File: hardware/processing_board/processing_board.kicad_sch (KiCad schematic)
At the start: 8 parts, among them J1 USB_C_Receptacle_USB2.0_14P, J2 USB_C_Receptacle_USB2.0_14P

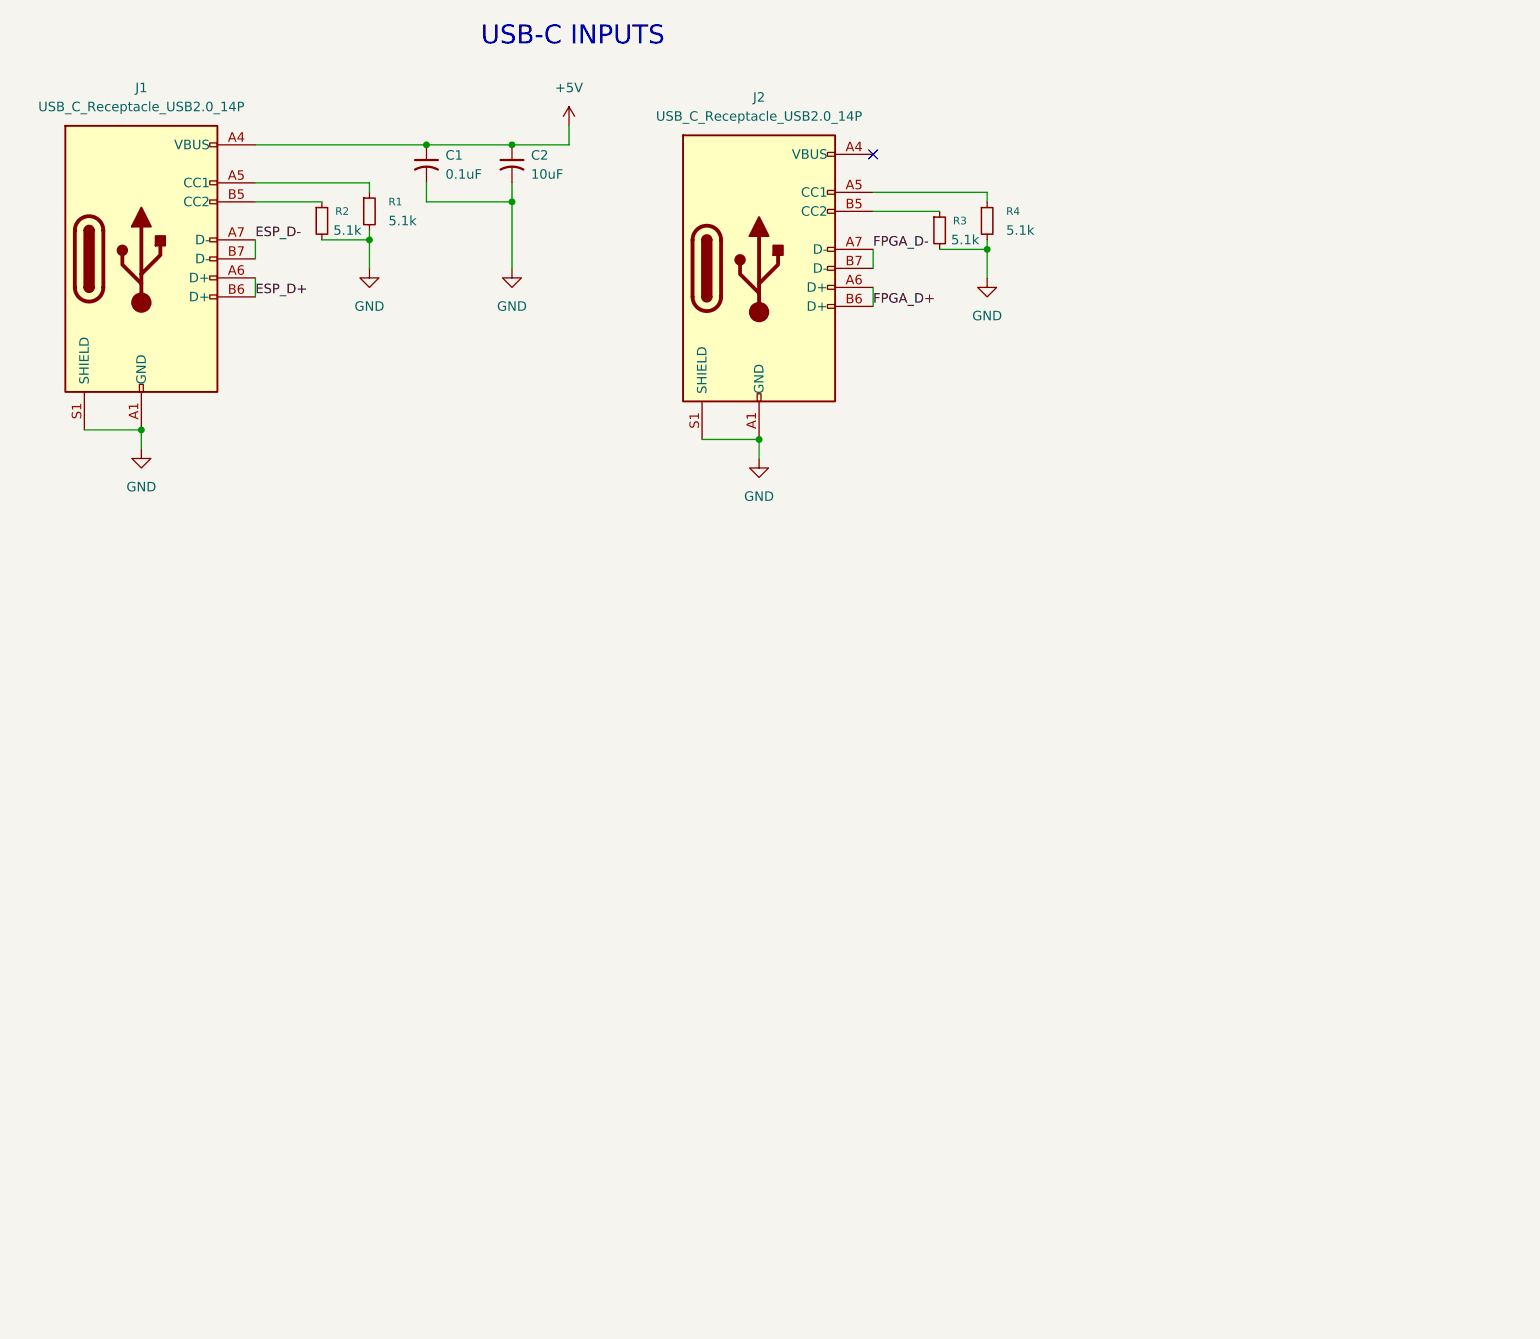
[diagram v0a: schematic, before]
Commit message: Added 3v3 LDO and 1V0 buck
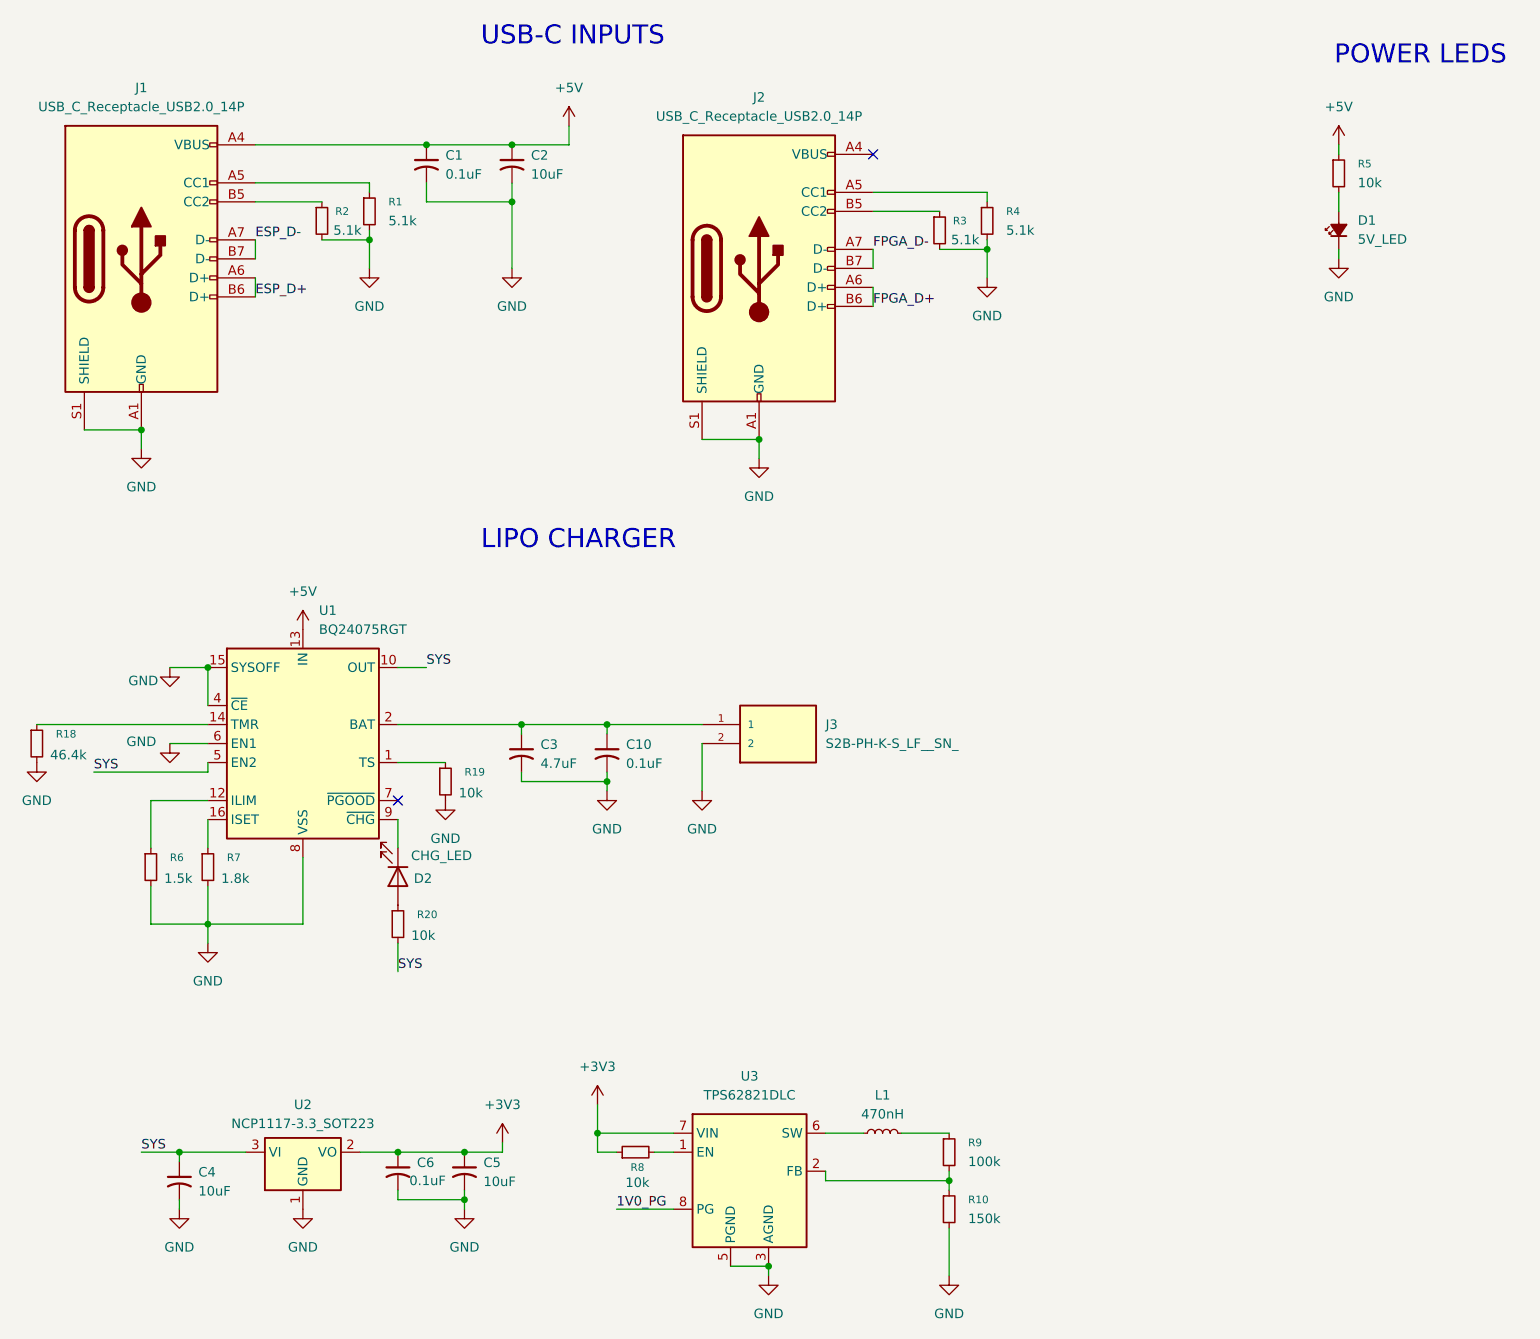
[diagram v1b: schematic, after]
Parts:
- added C10: 0.1uF, Capacitor_SMD:C_0805_2012Metric, symbol Device:C_Small_US
- added C3: 4.7uF, Capacitor_SMD:C_0805_2012Metric, symbol Device:C_Small_US
- added C4, C5: 10uF, symbol Device:C_Small_US
- added C6: 0.1uF, symbol Device:C_Small_US
- added D1: 5V_LED, symbol Device:LED_Small_Filled
- added D2: CHG_LED, LED_SMD:LED_0805_2012Metric, symbol Device:LED
- added J3: S2B-PH-K-S_LF__SN_, S2B-PH-K-S_LF__SN_:JST_S2B-PH-K-S_LF__SN_, symbol S2B-PH-K-S_LF__SN_:S2B-PH-K-S_LF__SN_
- added L1: 470nH, symbol Device:L_Small
- added R10: 150k, symbol Device:R_Small
- added R18: 46.4k, Resistor_SMD:R_0805_2012Metric, symbol Device:R_Small
- added R19, R20: 10k, Resistor_SMD:R_0805_2012Metric, symbol Device:R_Small
- added R5, R8: 10k, symbol Device:R_Small
- added R6: 1.5k, Resistor_SMD:R_0805_2012Metric, symbol Device:R_Small
- added R7: 1.8k, Resistor_SMD:R_0805_2012Metric, symbol Device:R_Small
- added R9: 100k, symbol Device:R_Small
- added U1: BQ24075RGT, Package_DFN_QFN:VQFN-16-1EP_3x3mm_P0.5mm_EP1.6x1.6mm, symbol Battery_Management:BQ24075RGT
- added U2: NCP1117-3.3_SOT223, Package_TO_SOT_SMD:SOT-223-3_TabPin2, symbol Regulator_Linear:NCP1117-3.3_SOT223
- added U3: TPS62821DLC, Package_SON:Texas_VSON-HR-8_1.5x2mm_P0.5mm, symbol Regulator_Switching:TPS62821DLC
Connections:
- net +5V: now also R5.1, U1.13 (IN)
- net GND: now also C10.2, C3.2, C4.2, C5.2, C6.2, D1.1 (K), J3.2, R10.2, R18.2, R19.2, R6.2, R7.2, U1.15 (SYSOFF), U1.17 (VSS), U1.4 (~{CE}), U1.6 (EN1), U1.8 (VSS), U2.1 (GND), U3.3 (AGND), U3.5 (PGND)
- new net: R8.2, U3.1 (EN)
- new net: R19.1, U1.1 (TS)
- new net: R6.1, U1.12 (ILIM)
- new net: R18.1, U1.14 (TMR)
- new net: R7.1, U1.16 (ISET)
- new net: C10.1, C3.1, J3.1, U1.2 (BAT), U1.3 (BAT)
- new net: D2.1 (K), U1.9 (~{CHG})
- new net: D2.2 (A), R20.1
- new net: D1.2 (A), R5.2
- new net: R10.1, R9.2, U3.2 (FB)
- new net: L1.1, U3.6 (SW)
- new net: L1.2, R9.1
- new net +3V3: C5.1, C6.1, R8.1, U2.2 (VO), U3.7 (VIN)
- new net 1V0_PG: U3.8 (PG)
- new net SYS: C4.1, R20.2, U1.10 (OUT), U1.11 (OUT), U1.5 (EN2), U2.3 (VI)
- no-connect marks 1 -> 2
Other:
- note added: "LIPO CHARGER"
- note added: "POWER LEDS"

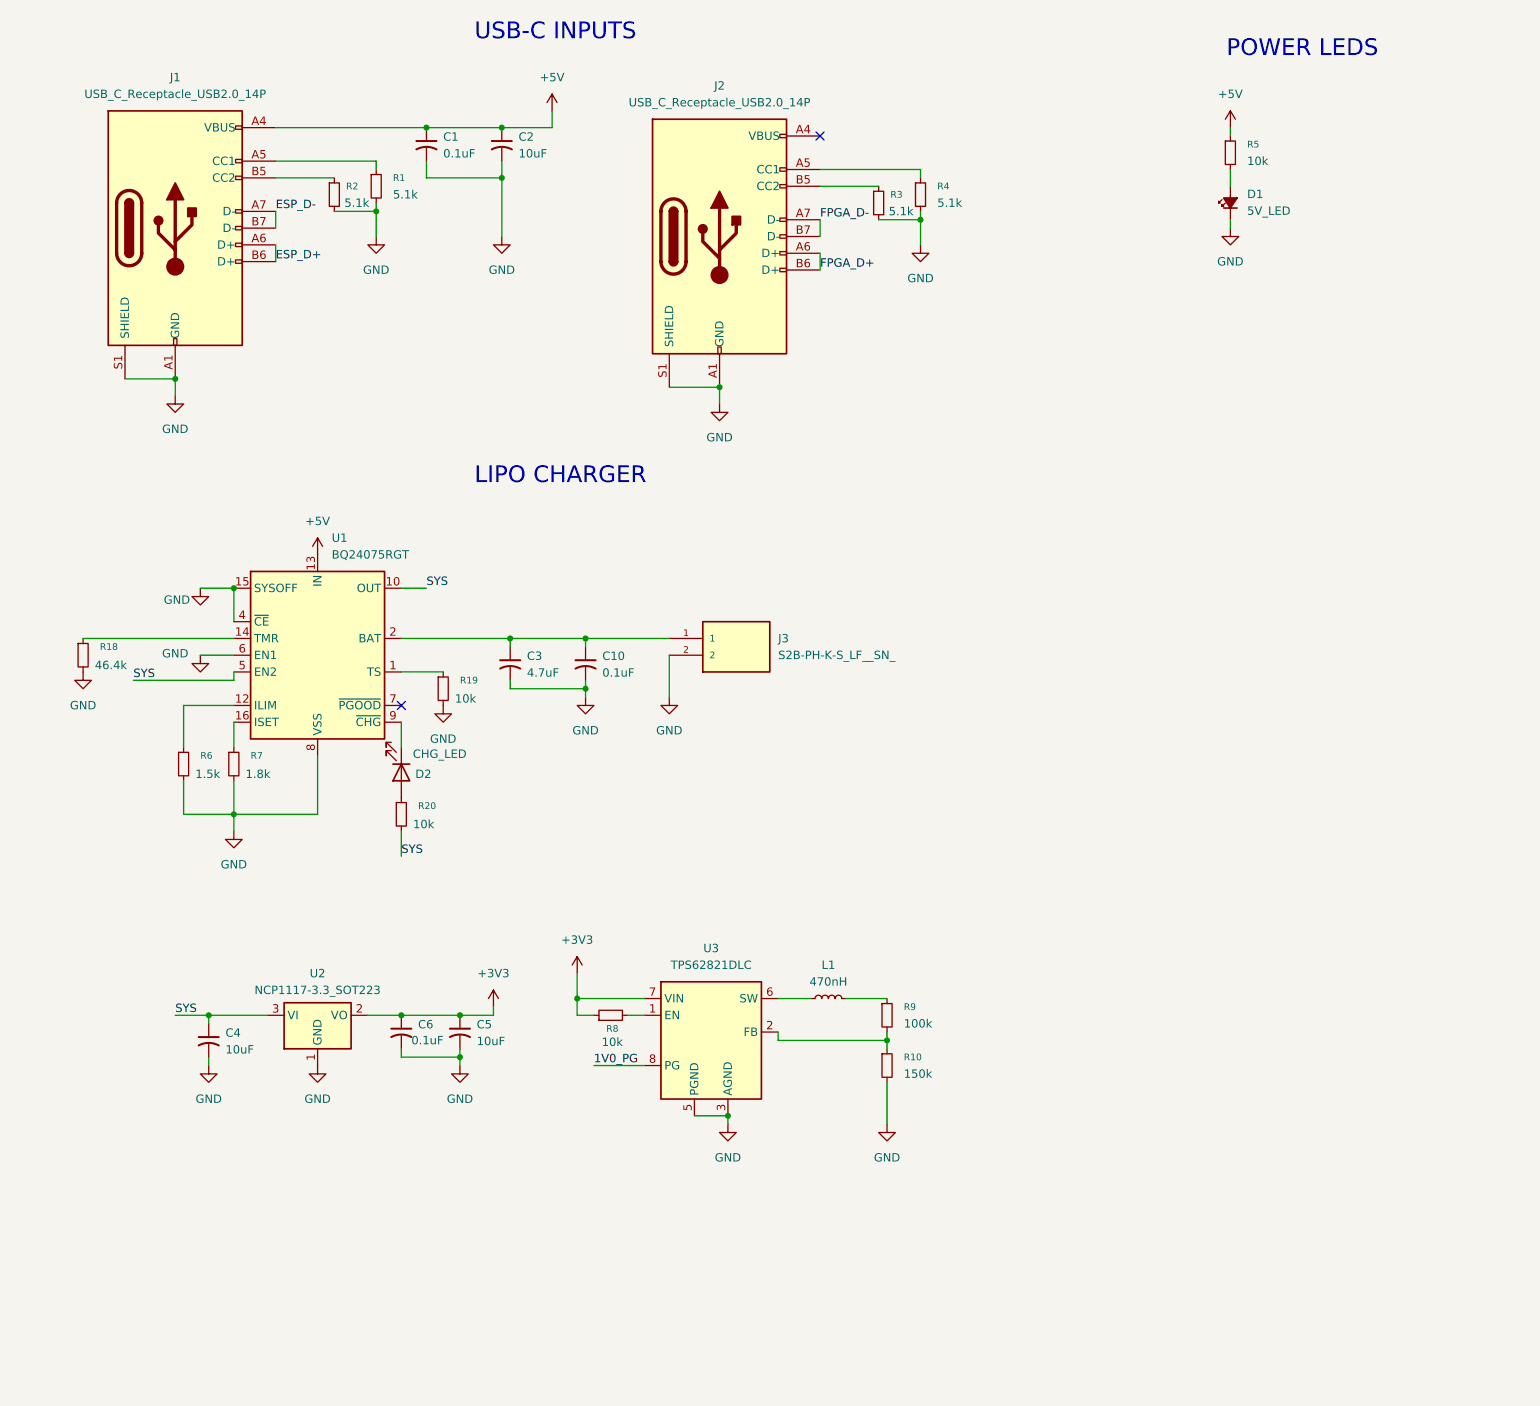
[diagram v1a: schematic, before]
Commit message: Full power tree added
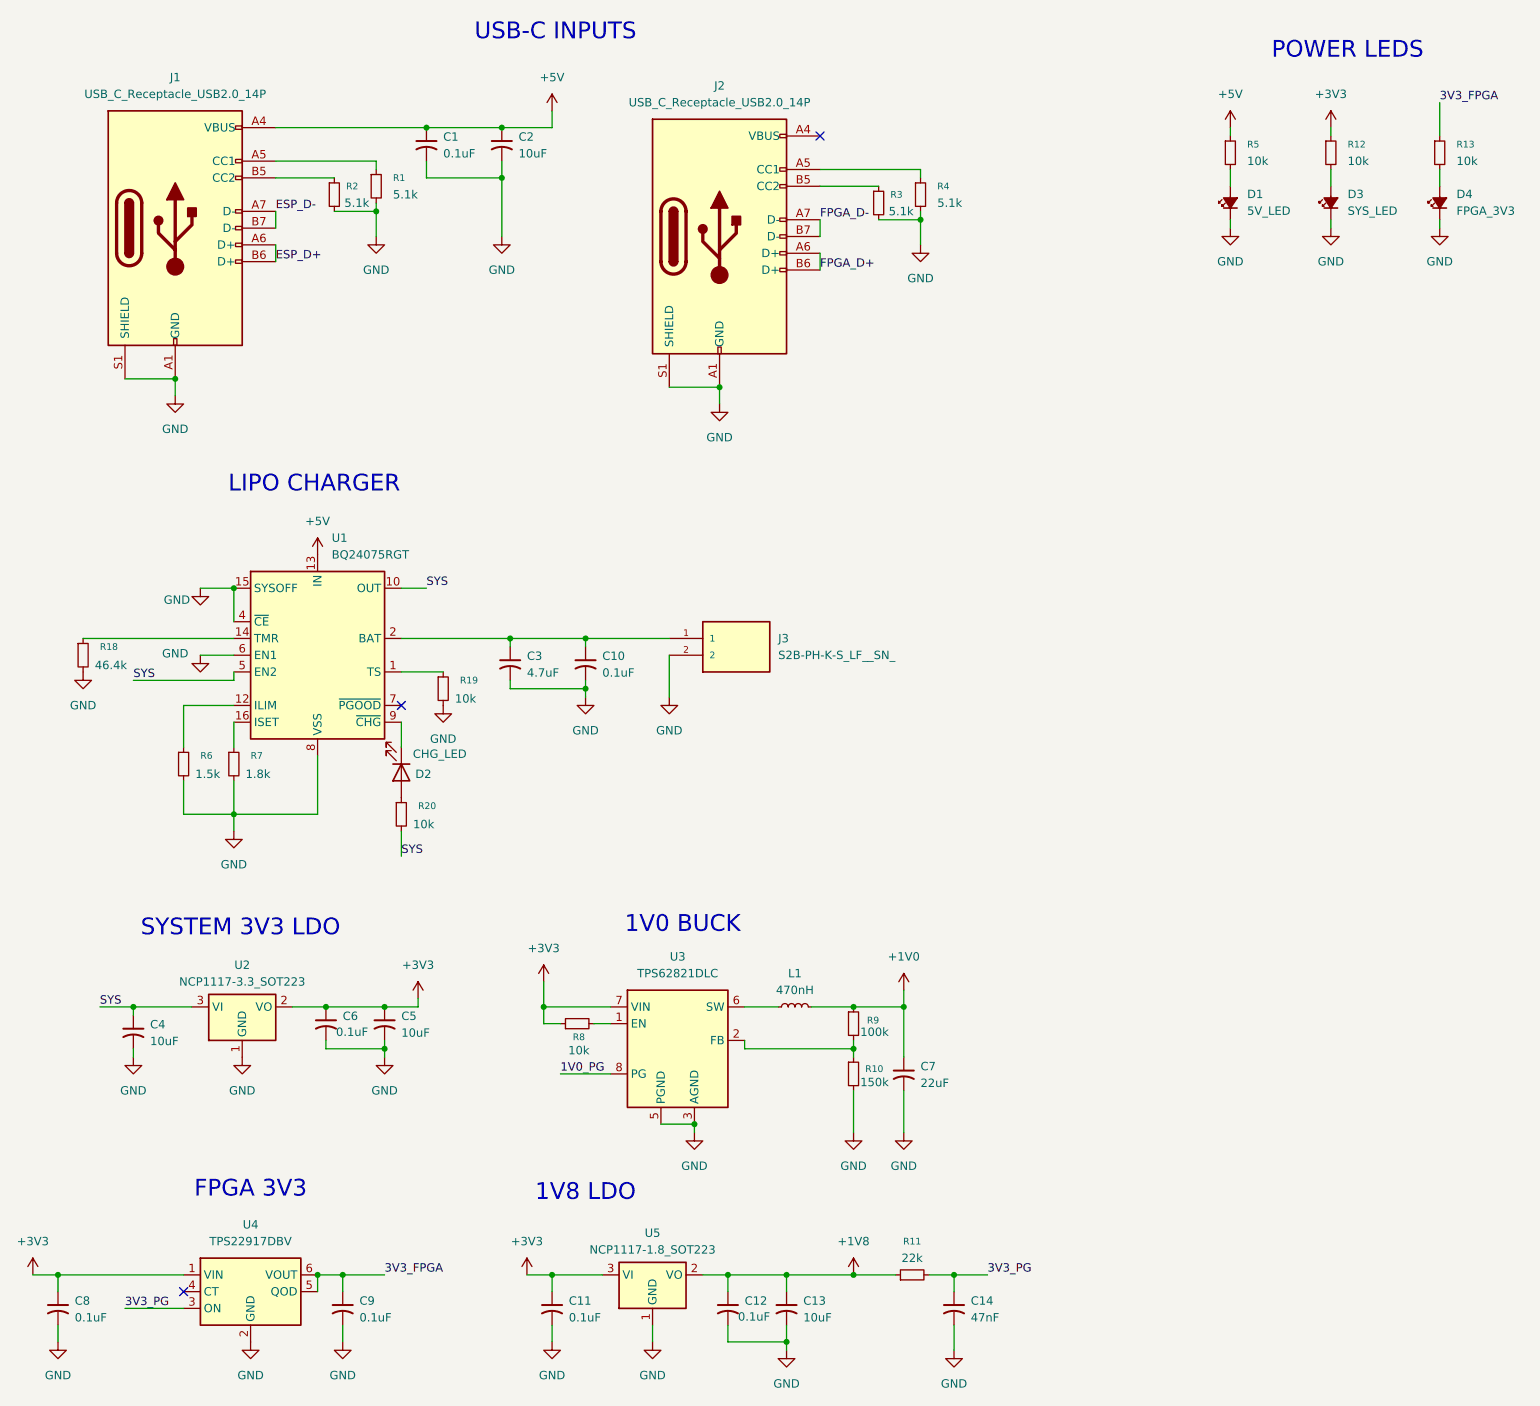
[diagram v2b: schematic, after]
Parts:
- added C11, C12, C8, C9: 0.1uF, symbol Device:C_Small_US
- added C13: 10uF, symbol Device:C_Small_US
- added C14: 47nF, symbol Device:C_Small_US
- added C7: 22uF, symbol Device:C_Small_US
- added D3: SYS_LED, symbol Device:LED_Small_Filled
- added D4: FPGA_3V3, symbol Device:LED_Small_Filled
- added R11: 22k, symbol Device:R_Small
- added R12, R13: 10k, symbol Device:R_Small
- added U4: TPS22917DBV, Package_TO_SOT_SMD:SOT-23-6, symbol Power_Management:TPS22917DBV
- added U5: NCP1117-1.8_SOT223, Package_TO_SOT_SMD:SOT-223-3_TabPin2, symbol Regulator_Linear:NCP1117-1.8_SOT223
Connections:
- net +3V3: now also C11.1, C8.1, R12.1, U4.1 (VIN), U5.3 (VI)
- net GND: now also C11.2, C12.2, C13.2, C14.2, C7.2, C8.2, C9.2, D3.1 (K), D4.1 (K), U4.2 (GND), U5.1 (GND)
- net +1V0: now reaches L1.2, R9.1
- net +1V0: now also C7.1
- new net: D4.2 (A), R13.2
- new net: D3.2 (A), R12.2
- new net +1V8: C12.1, C13.1, R11.1, U5.2 (VO)
- new net 3V3_FPGA: C9.1, R13.1, U4.5 (QOD), U4.6 (VOUT)
- new net 3V3_PG: C14.1, R11.2, U4.3 (ON)
- no-connect marks 2 -> 3
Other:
- note added: "1V0 BUCK"
- note added: "1V8 LDO"
- note added: "FPGA 3V3"
- note added: "SYSTEM 3V3 LDO"
- moved on the sheet: C4, C5, C6, L1, R10, R8, R9, U2, U3
